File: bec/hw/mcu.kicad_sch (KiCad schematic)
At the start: 2 parts, among them U1 STSPIN32F0

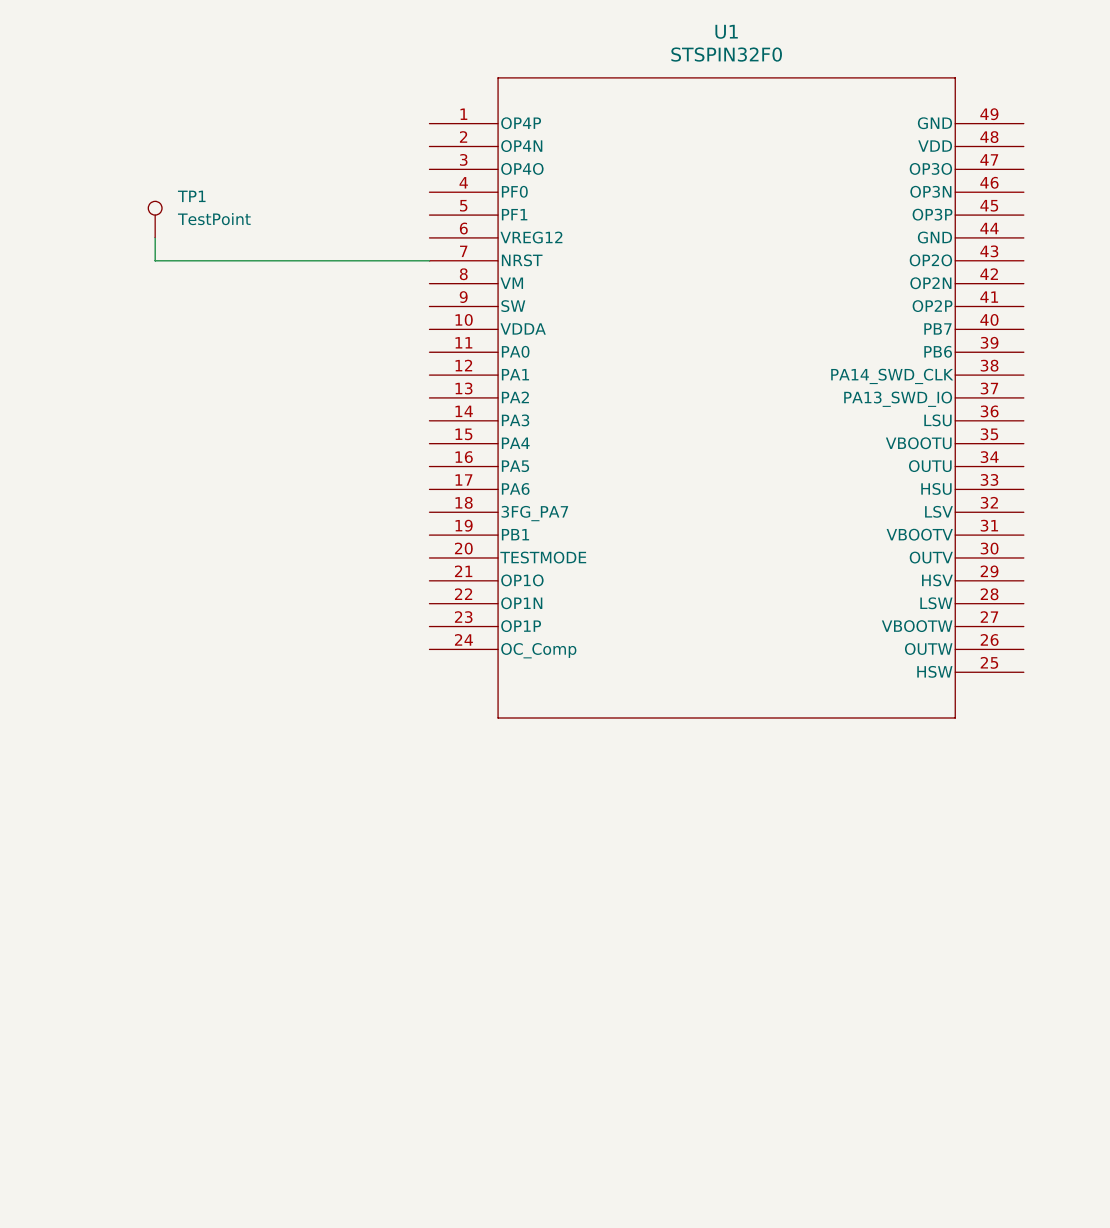
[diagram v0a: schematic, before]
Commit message: Started clarke-park transforms for ESC firmware
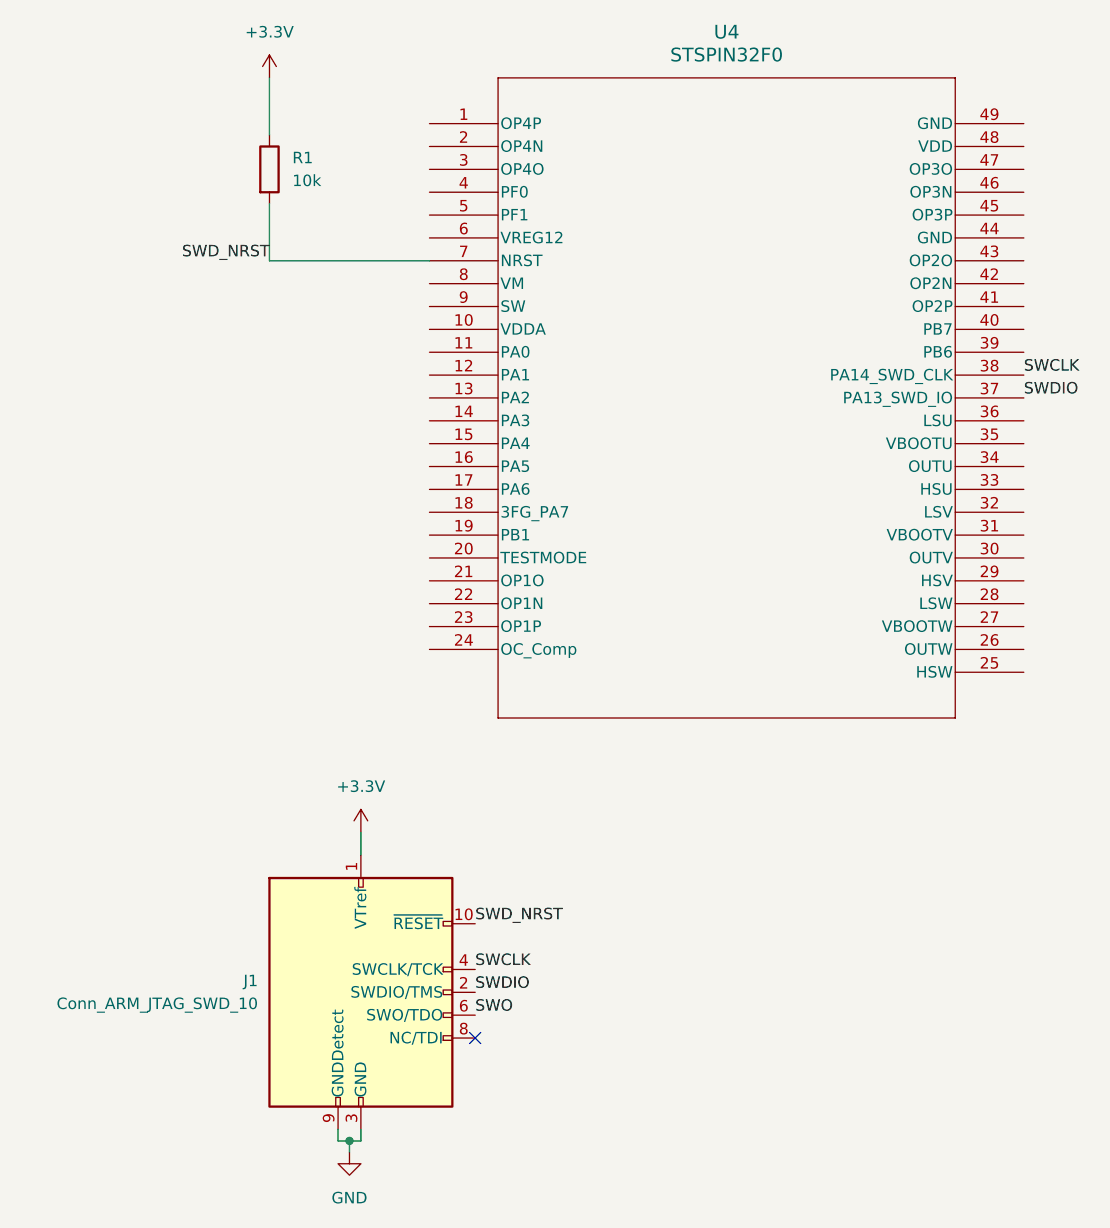
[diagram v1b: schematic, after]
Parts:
- removed TP1: TestPoint, TestPoint:TestPoint_Pad_1.0x1.0mm, symbol Connector:TestPoint
- added J1: Conn_ARM_JTAG_SWD_10, Connector_PinHeader_1.27mm:PinHeader_2x05_P1.27mm_Vertical, symbol Connector:Conn_ARM_JTAG_SWD_10
- added R1: 10k, Resistor_SMD:R_0805_2012Metric, symbol Device:R
- renumbered U1 to U4
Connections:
- net SWDIO: now reaches U4.37 (PA13_SWD_IO)
- net SWDIO: now also J1.2 (SWDIO/TMS)
- net SWCLK: now reaches U4.38 (PA14_SWD_CLK)
- net SWCLK: now also J1.4 (SWCLK/TCK)
- net SWD_NRST: now reaches U4.7 (NRST)
- net SWD_NRST: now also J1.10 (~{RESET}), R1.2
- new net +3.3V: J1.1 (VTref), R1.1
- new net GND: J1.3 (GND), J1.5 (GND), J1.9 (GNDDetect)
- new net SWO: J1.6 (SWO/TDO)
- no-connect marks 0 -> 1

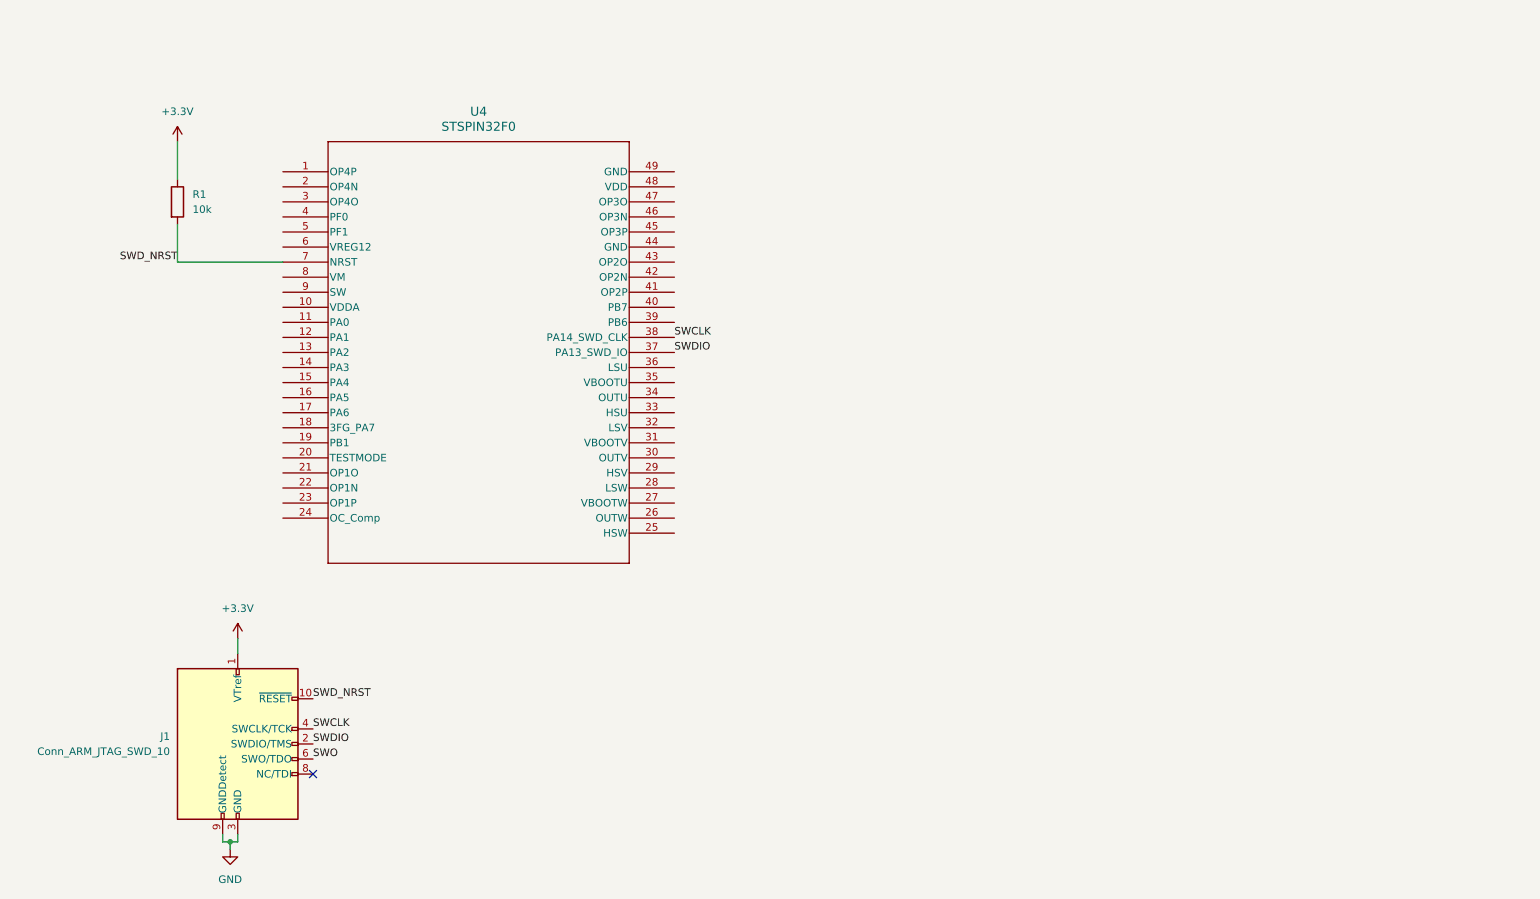
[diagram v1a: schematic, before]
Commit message: Added motor phase half bridges
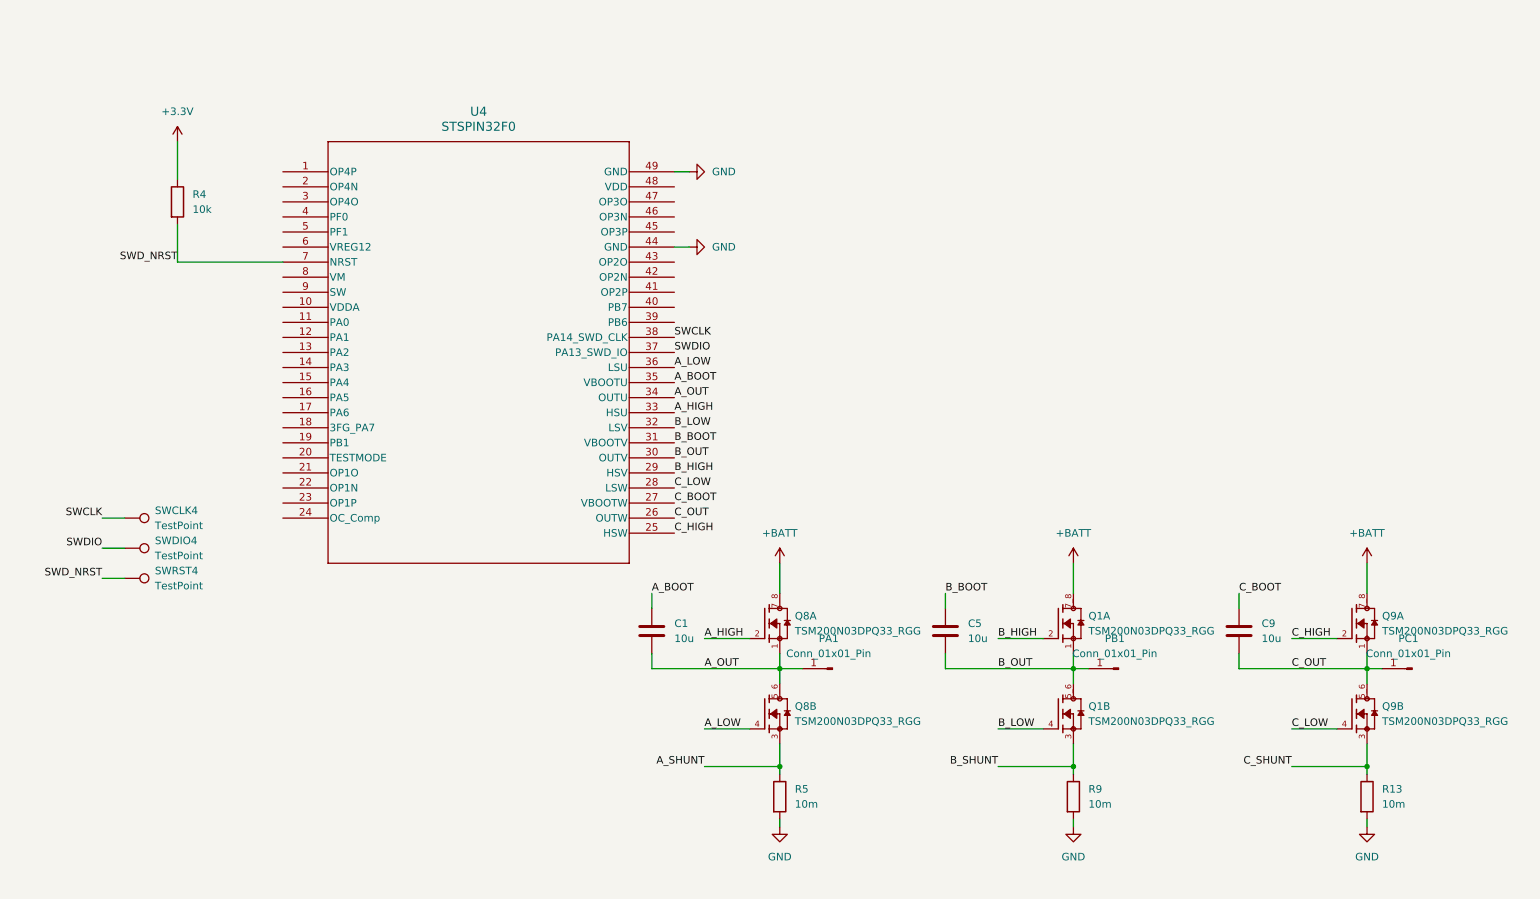
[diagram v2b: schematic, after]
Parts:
- removed J1: Conn_ARM_JTAG_SWD_10, Connector_PinHeader_1.27mm:PinHeader_2x05_P1.27mm_Vertical, symbol Connector:Conn_ARM_JTAG_SWD_10
- added C1, C5, C9: 10u, Capacitor_SMD:C_0805_2012Metric, symbol Device:C
- added PA1, PB1, PC1: Conn_01x01_Pin, symbol Connector:Conn_01x01_Pin
- added Q1, Q8, Q9: TSM200N03DPQ33_RGG, Snapeda:TSM200N03DPQ33_RGG_TRANS_TSM200N03DPQ33_RGG, symbol Snapeda:TSM200N03DPQ33_RGG
- added R13, R5, R9: 10m, Resistor_SMD:R_1210_3225Metric, symbol Device:R
- added SWCLK4, SWDIO4, SWRST4: TestPoint, TestPoint:TestPoint_Pad_D1.0mm, symbol Connector:TestPoint
- renumbered R1 to R4
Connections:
- net GND: now also U4.44 (GND), U4.49 (GND), R13.2, R5.2, R9.2
- net SWCLK: now also SWCLK4.1
- net SWDIO: now also SWDIO4.1
- net SWD_NRST: now also SWRST4.1
- net C_HIGH: now reaches U4.25 (HSW)
- net C_HIGH: now also Q9.2
- net C_OUT: now reaches U4.26 (OUTW)
- net C_OUT: now also C9.2, PC1.1 (Pin_1), Q9.1, Q9.5_6
- net C_BOOT: now reaches U4.27 (VBOOTW)
- net C_BOOT: now also C9.1
- net C_LOW: now reaches U4.28 (LSW)
- net C_LOW: now also Q9.4
- net B_HIGH: now reaches U4.29 (HSV)
- net B_HIGH: now also Q1.2
- net B_OUT: now reaches U4.30 (OUTV)
- net B_OUT: now also C5.2, PB1.1 (Pin_1), Q1.1, Q1.5_6
- net B_BOOT: now reaches U4.31 (VBOOTV)
- net B_BOOT: now also C5.1
- net B_LOW: now reaches U4.32 (LSV)
- net B_LOW: now also Q1.4
- net A_HIGH: now reaches U4.33 (HSU)
- net A_HIGH: now also Q8.2
- net A_OUT: now reaches U4.34 (OUTU)
- net A_OUT: now also C1.2, PA1.1 (Pin_1), Q8.1, Q8.5_6
- net A_BOOT: now reaches U4.35 (VBOOTU)
- net A_BOOT: now also C1.1
- net A_LOW: now reaches U4.36 (LSU)
- net A_LOW: now also Q8.4
- new net +BATT: Q1.7_8, Q8.7_8, Q9.7_8
- new net A_SHUNT: Q8.3, R5.1
- new net B_SHUNT: Q1.3, R9.1
- new net C_SHUNT: Q9.3, R13.1
- no-connect marks 1 -> 0

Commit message: Added TPS54331 for 3.3v supply
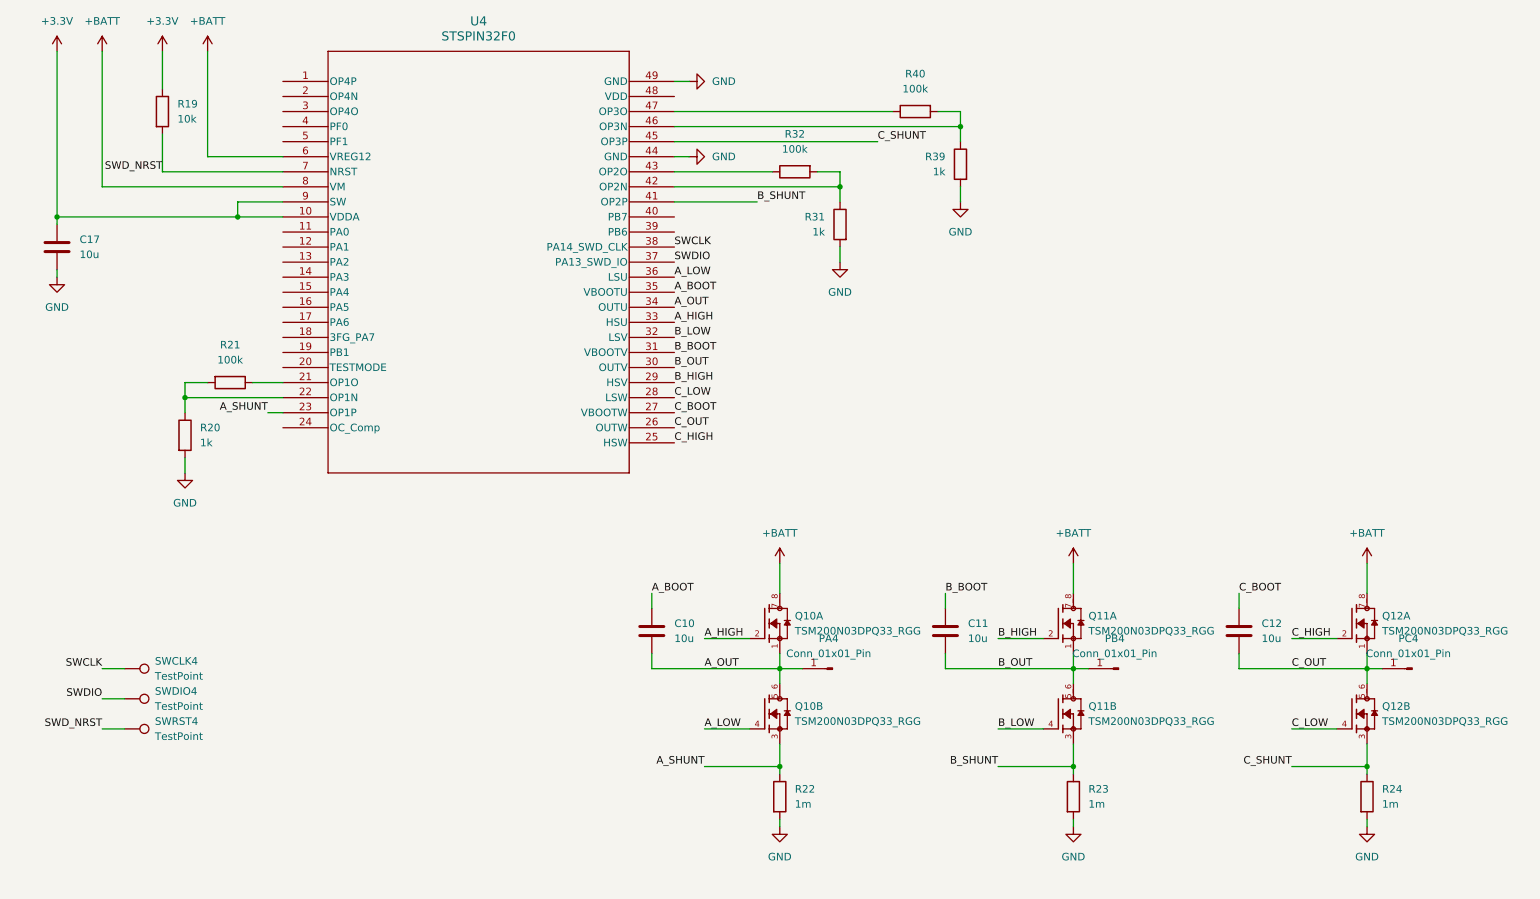
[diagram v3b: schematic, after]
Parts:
- added C17: 10u, Capacitor_SMD:C_0805_2012Metric, symbol Device:C
- added R20, R31, R39: 1k, Resistor_SMD:R_0805_2012Metric, symbol Device:R
- added R21, R32, R40: 100k, Resistor_SMD:R_0805_2012Metric, symbol Device:R
- R22: renamed from R5; value 10m -> 1m
- R23: renamed from R9; value 10m -> 1m
- R24: renamed from R13; value 10m -> 1m
- renumbered C1 to C10, C5 to C11, C9 to C12, PA1 to PA4, PB1 to PB4, PC1 to PC4, Q8 to Q10, Q1 to Q11, Q9 to Q12, R4 to R19
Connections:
- net +3.3V: now also U4.10 (VDDA), U4.9 (SW), C17.1
- net +BATT: now also U4.6 (VREG12), U4.8 (VM)
- net A_SHUNT: now also U4.23 (OP1P)
- net B_SHUNT: now also U4.41 (OP2P)
- net C_SHUNT: now also U4.45 (OP3P)
- net GND: now also C17.2, R20.2, R31.2, R39.2
- net at U4.21 (OP1O): now also R21.1
- net at U4.22 (OP1N): now also R20.1, R21.2
- net at U4.42 (OP2N): now also R31.1, R32.2
- net at U4.43 (OP2O): now also R32.1
- net at U4.46 (OP3N): now also R39.1, R40.2
- net at U4.47 (OP3O): now also R40.1
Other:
- moved on the sheet: R19, SWCLK4, SWDIO4, SWRST4, U4
